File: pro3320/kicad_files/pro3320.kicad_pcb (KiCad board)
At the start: 2 copper layers, 94 parts, among them J1 RES_CV_IN, J2 AUDIO_IN, J3 FREQ_CV_IN, J4 EUROPOWER, J5 OUT_MAIN, J6 OUT_3, J7 OUT_2, J8 OUT_1, SW1 LP_HP_CAP_2, SW2 LP_HP_1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

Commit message: pro3320: Abandon panel PCB
I tried having a PCB parallell to the panel, but it gets too
wide for my taste (and/or requires too much time and brain
activity in the PCB layout tool).

Will slim it down, having the PCB hanging on the pots, and
mounting the jacks on panel, the switches as well, having
to solder a LOT of cables. It will be hell, but I don't see
another way (except having two PCBs, layered, but that's too
much for me now).
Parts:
- C12, C13, C2, C3: value 300p -> 150p
- J1: value RES_CV_IN -> RES_CV
- J2: value AUDIO_IN -> IN
- J3: value FREQ_CV_IN -> FREQ_CV
- J5: value OUT_MAIN -> OUT
- J6, J7: moved to B.Cu
- moved C3 275.8 mm to (6.35, 109.0), turned to 180 degrees
- moved C10 268.1 mm to (20.3, 126.7)
- moved C11 250.3 mm to (20.3, 122.2)
- moved C12 245.2 mm to (20.6, 116.1)
- moved C2 240.0 mm to (6.35, 104.4), turned to 180 degrees
- moved R26 223.0 mm to (20.1, 98.3)
- moved R29 221.6 mm to (41.7, 126.5)
- moved R27 220.9 mm to (36.3, 168.1)
- moved C13 217.0 mm to (25.4, 103.4), turned to 180 degrees
- moved R28 207.8 mm to (52.6, 112.3)
- moved R31 207.8 mm to (56.0, 109.3)
- moved R32 203.4 mm to (79.5, 128.0)
- moved R36 197.9 mm to (79.5, 131.1)
- moved C16 189.0 mm to (106.2, 164.8)
- moved C17 189.0 mm to (103.6, 152.1)
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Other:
- board outline added: 87.6 x 99.1 mm

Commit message: pro3320: First messy PCB attempt
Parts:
- removed C16, C17: 2.2uF, Capacitor_THT:CP_Radial_D5.0mm_P2.00mm
- removed J7: OUT_2, kicadlib:PJ301BM
- removed J8: OUT_1, kicadlib:PJ301BM
- removed R35: 100k, Resistor_THT:R_Axial_DIN0207_L6.3mm_D2.5mm_P7.62mm_Horizontal
- removed R37, R38, R39: 240k, Resistor_THT:R_Axial_DIN0207_L6.3mm_D2.5mm_P7.62mm_Horizontal
- removed R41, R42, R43, R45, R46, R47: 2.2k, Resistor_THT:R_Axial_DIN0207_L6.3mm_D2.5mm_P7.62mm_Horizontal
- removed SW5: LP_HP_3, kicadlib:DPDT_PUSH_SW
- removed SW6: LP_HP_CAP_4, kicadlib:DPDT_AS_SPDT_PUSH_SW
- removed SW7: LP_HP_4, kicadlib:DPDT_PUSH_SW
- added JP1: OPT_OUT2, Connector_PinHeader_2.54mm:PinHeader_1x02_P2.54mm_Vertical, F.Cu at (113.5, 117.9)
- added REF**: , MountingHole:MountingHole_3.2mm_M3, F.Cu at (152.1, 123.4)
- added REF**: , MountingHole:MountingHole_3.2mm_M3, F.Cu at (152.1, 56.9)
- added REF**: , kicadlib:mod_area_17x07, F.Cu at (99.6, 71.1)
- C10: value 100nF -> 2.2uF; footprint Capacitor_THT:C_Rect_L7.2mm_W3.5mm_P5.00mm_FKS2_FKP2_MKS2_MKP2 -> Capacitor_THT:CP_Radial_D5.0mm_P2.00mm
- C15: value 2.2uF -> 100nF; footprint Capacitor_THT:CP_Radial_D5.0mm_P2.00mm -> Capacitor_THT:C_Rect_L7.2mm_W3.5mm_P5.00mm_FKS2_FKP2_MKS2_MKP2
- J1, J2, J3, J5: footprint kicadlib:PJ301BM -> Connector_PinHeader_2.54mm:PinHeader_1x03_P2.54mm_Vertical; moved to F.Cu
- J4: moved to F.Cu
- J6: value OUT_3 -> OUT2; footprint kicadlib:PJ301BM -> Connector_PinHeader_2.54mm:PinHeader_1x03_P2.54mm_Vertical; moved to F.Cu
- R34: value 100k -> 240k
- RV1, RV2, RV3, RV4, RV5: footprint Potentiometer_THT:Potentiometer_Alps_RK09K_Single_Vertical -> Potentiometer_THT:Potentiometer_Alps_RK097_Single_Horizontal
- SW1: value LP_HP_CAP_2 -> LPHP2; footprint kicadlib:DPDT_AS_SPDT_PUSH_SW -> Connector_PinHeader_2.54mm:PinHeader_1x09_P2.54mm_Vertical; moved to F.Cu
- SW2: value LP_HP_1 -> LPHP1; footprint kicadlib:DPDT_PUSH_SW -> Connector_PinHeader_2.54mm:PinHeader_1x06_P2.54mm_Vertical; moved to F.Cu
- SW3: value LP_HP_2 -> LPHP3; footprint kicadlib:DPDT_PUSH_SW -> Connector_PinHeader_2.54mm:PinHeader_1x09_P2.54mm_Vertical; moved to F.Cu
- SW4: value LP_HP_CAP_3 -> LPHP4; footprint kicadlib:DPDT_AS_SPDT_PUSH_SW -> Connector_PinHeader_2.54mm:PinHeader_1x09_P2.54mm_Vertical; moved to F.Cu
- TP1, TP2: footprint TestPoint:TestPoint_THTPad_3.0x3.0mm_Drill1.5mm -> TestPoint:TestPoint_THTPad_2.0x2.0mm_Drill1.0mm
- TP3: value OUT_STAGE_4 -> OUT_STAGE_3; footprint TestPoint:TestPoint_THTPad_3.0x3.0mm_Drill1.5mm -> TestPoint:TestPoint_THTPad_2.0x2.0mm_Drill1.0mm
- TP4: value OUT_STAGE_3 -> OUT_STAGE_4; footprint TestPoint:TestPoint_THTPad_3.0x3.0mm_Drill1.5mm -> TestPoint:TestPoint_THTPad_2.0x2.0mm_Drill1.0mm
- U3: value TL074 -> TL072; footprint Package_DIP:DIP-14_W7.62mm -> Package_DIP:DIP-8_W7.62mm
- moved C6 147.3 mm to (110.5, 55.4), turned to 180 degrees
- moved R24 144.6 mm to (95.5, 75.9), turned to 270 degrees
- moved R20 131.4 mm to (125.5, 77.7), turned to 0 degrees
- moved C7 131.4 mm to (132.1, 69.1), turned to 180 degrees
- moved R26 121.4 mm to (141.5, 95.8), turned to 270 degrees
- moved R23 119.6 mm to (125.5, 81.3), turned to 0 degrees
- moved C4 117.8 mm to (99.3, 127.0)
- moved U2 116.1 mm to (125.0, 85.1)
- moved C2 114.9 mm to (120.4, 90.7), turned to 90 degrees
- moved C3 114.5 mm to (120.4, 98.6), turned to 90 degrees
- moved R21 111.5 mm to (137.9, 95.8), turned to 270 degrees
- moved C5 106.7 mm to (107.2, 126.0), turned to 270 degrees
- moved J4 104.7 mm to (94.0, 137.2), turned to 180 degrees
- moved C9 103.5 mm to (141.7, 111.8), turned to 90 degrees
- moved R13 102.9 mm to (112.8, 50.8), turned to 0 degrees
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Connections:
- C10 pad 1: +12V -> Net-(C10-Pad1)
- C10 pad 2: GND -> Net-(C10-Pad2)
- C11 pad 1: GND -> +12V
- C11 pad 2: -12V -> GND
- C15 pad 1: Net-(C15-Pad1) -> GND
- C15 pad 2: Net-(C15-Pad2) -> -12V
- R20 pad 1: Net-(C16-Pad1) -> Net-(JP1-Pad1)
- R24 pad 1: Net-(C16-Pad1) -> Net-(JP1-Pad1)
- R28 pad 2: Net-(C15-Pad1) -> Net-(R28-Pad2)
- R31 pad 1: Net-(C15-Pad1) -> Net-(R28-Pad2)
- R34 pad 1: Net-(R34-Pad1) -> Net-(J6-Pad3)
- R34 pad 2: GND -> Net-(R33-Pad1)
- SW3 pad 1: Net-(R20-Pad2) -> GND
- SW3 pad 2: Net-(R14-Pad1) -> Net-(C13-Pad1)
- SW3 pad 3: (no net) -> Net-(JP1-Pad1)
- SW3 pad 4: Net-(R15-Pad1) -> Net-(R28-Pad1)
- SW3 pad 5: Net-(R20-Pad2) -> Net-(R24-Pad2)
- SW4 pad 2: Net-(C13-Pad1) -> Net-(C12-Pad2)
- SW4 pad 3: Net-(C16-Pad1) -> Net-(R28-Pad2)
- TP2 pad 1: Net-(C16-Pad1) -> Net-(JP1-Pad1)
- TP3 pad 1: Net-(C14-Pad1) -> Net-(R28-Pad2)
- TP4 pad 1: Net-(C15-Pad1) -> Net-(C14-Pad1)
- U2 pad 15: Net-(C15-Pad1) -> Net-(R28-Pad2)
- U2 pad 6: Net-(C16-Pad1) -> Net-(JP1-Pad1)
- U3 pad 4: +12V -> -12V
- U3 pad 5: Net-(C15-Pad2) -> Net-(C10-Pad2)
- U3 pad 7: Net-(R37-Pad1) -> Net-(J6-Pad3)
- U3 pad 8: Net-(R38-Pad1) -> +12V
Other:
- board size 87.6 x 99.1 mm -> 68.3 x 99.1 mm

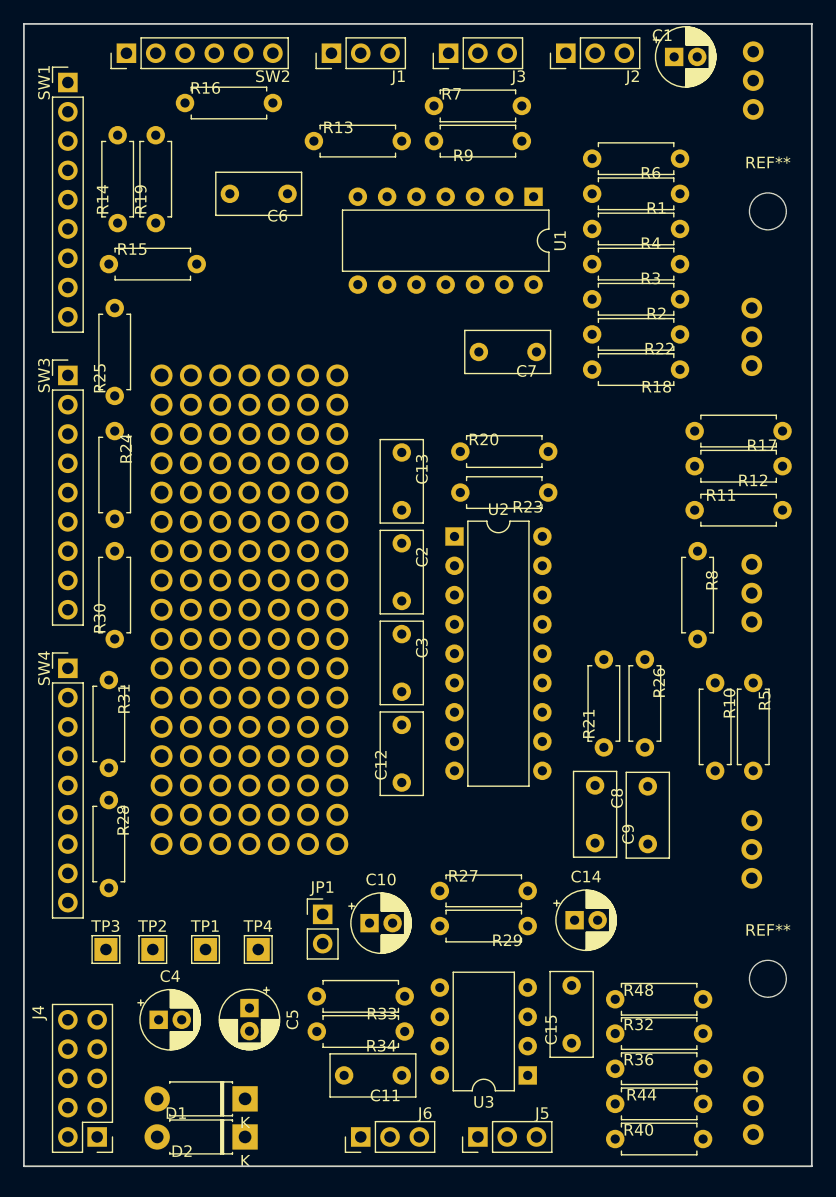
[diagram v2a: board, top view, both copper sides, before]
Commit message: pro3320: Finish PCB routing
It's not pretty, but will hopefully work.
There is something missing in my layout knowledge,I believe;
it feels like a better layout would make routing easier.
Whatevs.
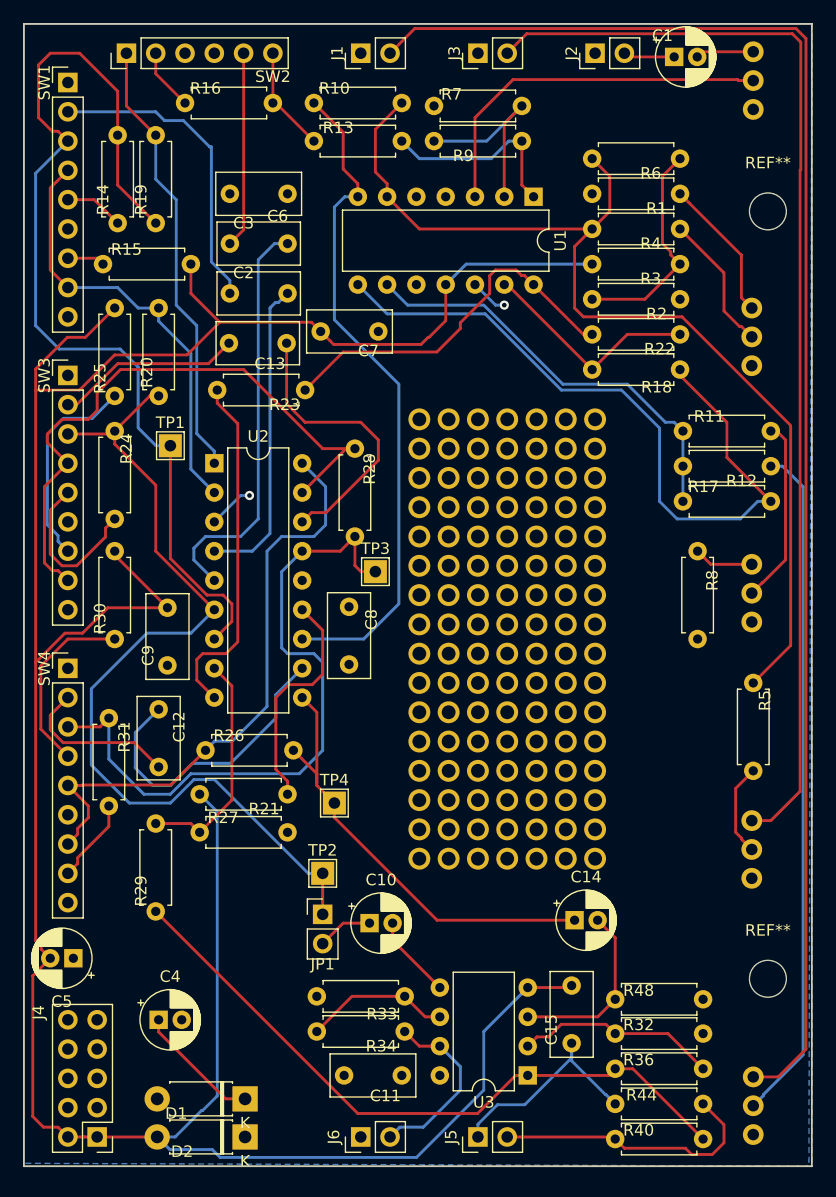
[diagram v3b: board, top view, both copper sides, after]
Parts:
- removed the REF** at (99.6, 71.1)
- added REF**: , kicadlib:mod_area_16x07, F.Cu at (121.9, 74.9)
- J1, J2, J3, J5, J6: footprint Connector_PinHeader_2.54mm:PinHeader_1x03_P2.54mm_Vertical -> Connector_PinHeader_2.54mm:PinHeader_1x02_P2.54mm_Vertical
- moved R10 61.2 mm to (112.8, 47.5), turned to 0 degrees
- moved C9 44.4 mm to (100.1, 96.3)
- moved TP1 43.8 mm to (100.3, 77.2)
- moved TP3 40.2 mm to (118.1, 88.1)
- moved C3 40.1 mm to (110.5, 59.7), turned to 180 degrees
- moved R26 38.9 mm to (103.4, 103.6), turned to 0 degrees
- moved R28 37.2 mm to (116.3, 77.5)
- moved R21 36.9 mm to (102.9, 107.4), turned to 0 degrees
- moved R29 32.3 mm to (99.1, 117.6), turned to 90 degrees
- moved C2 28.5 mm to (110.5, 64.0), turned to 180 degrees
- moved R20 26.6 mm to (99.3, 72.9), turned to 90 degrees
- moved C8 26.4 mm to (115.8, 91.2)
- moved R23 22.9 mm to (104.4, 72.4)
- moved C12 22.0 mm to (99.3, 100.1), turned to 270 degrees
- moved U2 21.8 mm to (104.1, 78.7)
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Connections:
- J1 pad 2: (no net) -> Net-(J1-Pad2)
- J2 pad 2: (no net) -> Net-(C1-Pad1)
- J3 pad 2: (no net) -> Net-(J3-Pad2)
- J5 pad 2: (no net) -> Net-(J5-Pad2)
- J6 pad 2: (no net) -> Net-(J6-Pad2)
- R34 pad 1: Net-(J6-Pad3) -> Net-(J6-Pad2)
- R40 pad 1: Net-(J5-Pad3) -> Net-(J5-Pad2)
- R44 pad 2: Net-(J5-Pad3) -> Net-(J5-Pad2)
- RV2 pad 1: Net-(J3-Pad3) -> Net-(J3-Pad2)
- RV3 pad 1: Net-(J1-Pad3) -> Net-(J1-Pad2)
- U3 pad 7: Net-(J6-Pad3) -> Net-(J6-Pad2)
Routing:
- net -12V: track 0.00 -> 248.3 mm
- net Net-(J1-Pad2): track 0.00 -> 130.5 mm
- net Net-(J3-Pad2): track 0.00 -> 96.7 mm
- net Net-(R10-Pad2): track 0.00 -> 89.8 mm
- net Net-(R14-Pad2): track 0.00 -> 86.1 mm
- net Net-(JP1-Pad1): track 0.00 -> 77.6 mm
- net Net-(R17-Pad2): track 0.00 -> 63.3 mm
- net Net-(R28-Pad2): track 0.00 -> 59.2 mm
- net Net-(R12-Pad1): track 0.00 -> 59.0 mm
- net Net-(R29-Pad1): track 0.00 -> 58.9 mm
- net Net-(R10-Pad1): track 0.00 -> 58.5 mm
- net Net-(R28-Pad1): track 0.00 -> 54.3 mm
- net Net-(R26-Pad1): track 0.00 -> 52.3 mm
- net Net-(C14-Pad1): track 0.00 -> 39.7 mm
- net Net-(R19-Pad2): track 0.00 -> 38.7 mm
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- added copper zone on B.Cu, net +12V
- added copper zone on F.Cu, net GND

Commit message: pro3320: Add logo to PCB
Also, polishing the PCB and schematic a wee bit.
Faced with the choice, what would you say?
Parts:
- added G***: LOGO, kicadlib:esm_logo_96x49mm, B.Cu at (125.7, 91.9)
- TP1: value OUT_STAGE_1 -> OP1
- TP2: value OUT_STAGE_2 -> OP2
- TP3: value OUT_STAGE_3 -> OP3
- TP4: value OUT_STAGE_4 -> OP4
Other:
- board text added: "A"
- board text added: "A VCF based on the CEM3320 data sheet reference manuals, with some inspo from the ProOne’s implementation."
- board text added: "April 16, 2019"
- board text added: "pro3320 vcf"
- board text added: "pro3320 vcf, rev A electronic sound machines 2019 Håkan Eriksson uheriks@yahoo.ca"
- board text added: "the path of least resistance"
